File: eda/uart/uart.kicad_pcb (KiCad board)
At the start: 2 copper layers, 122.6 x 85.1 mm, 48 parts, among them J1 UART, J2 Bus expansion, U1 74HCT08, U10 74HCT574, U11 74HCT595, U12 74HCT595, U13 CD74HCT40105E, U14 CD74HCT40105E, U16 74HCT14, U17 74HCT193, U18 74HCT32, U2 74HCT14, U3 74HCT193, U4 74HCT193, U5 74HCT165, U6 74HCT165, U7 74HCT139, U8 CD74HCT40105E, U9 CD74HCT40105E, X1 1.8xx

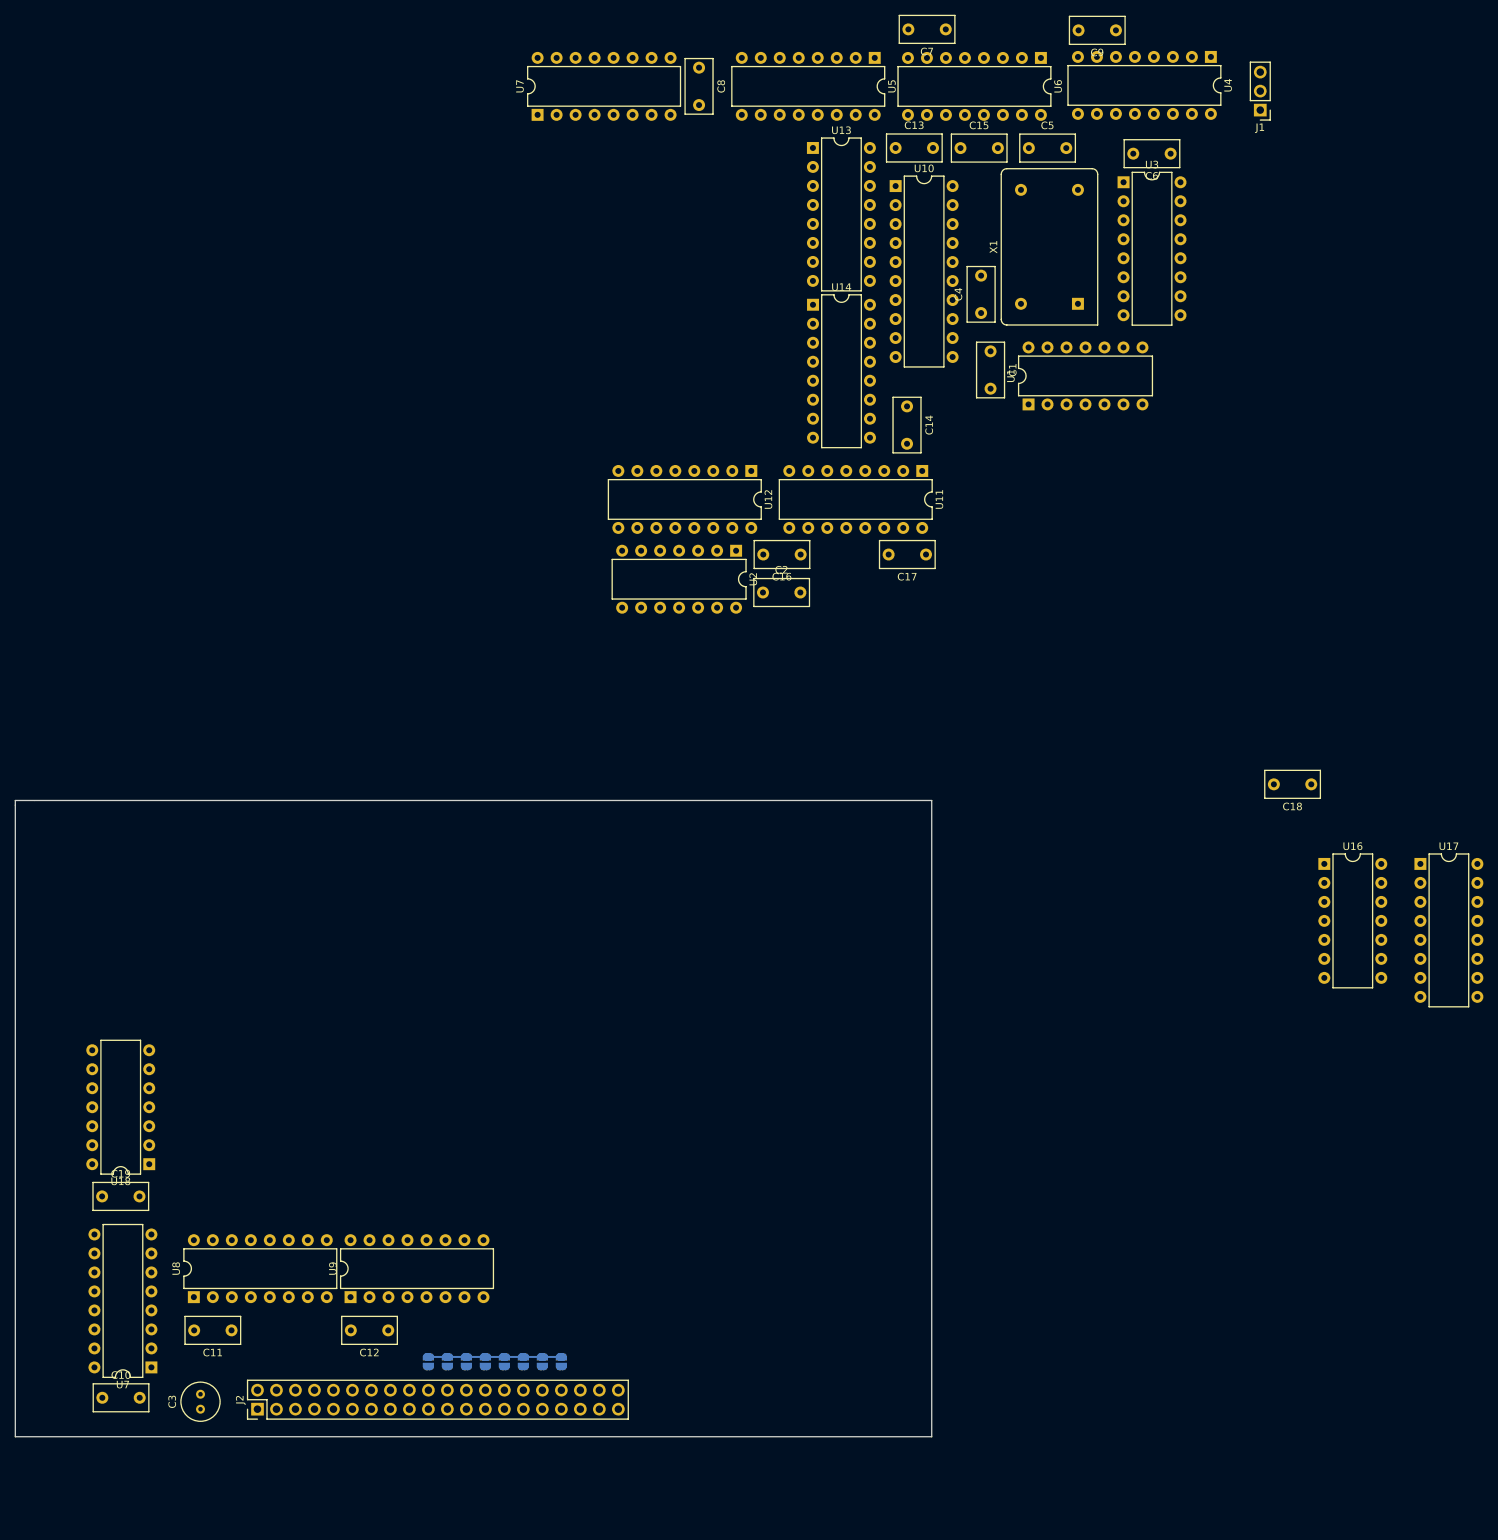
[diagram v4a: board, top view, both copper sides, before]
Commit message: Convert expansion breakout to kicad
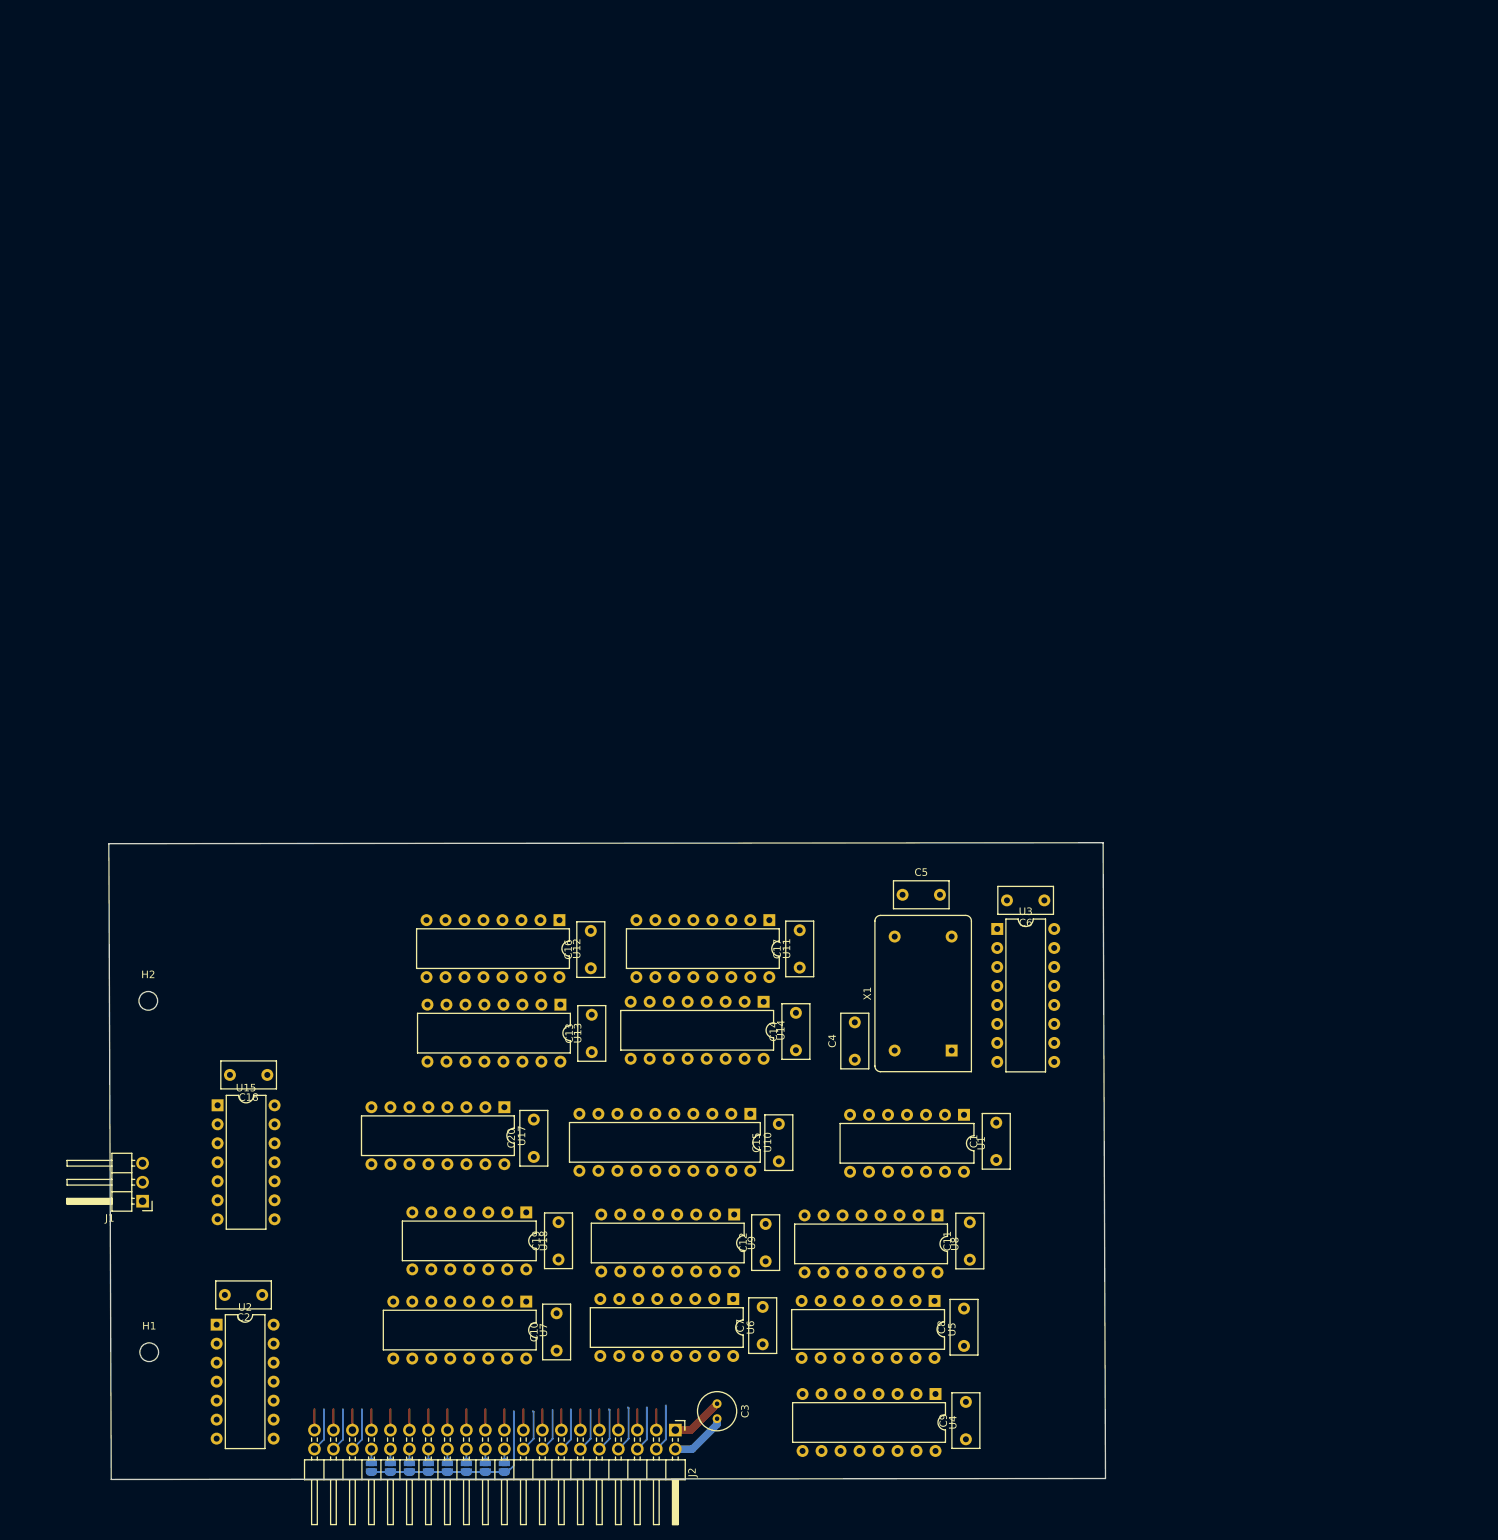
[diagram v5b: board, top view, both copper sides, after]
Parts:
- removed U16: 74HCT14, Package_DIP:DIP-14_W7.62mm
- removed the U7 at (95.9, -30.1)
- added C20: 0.1uf, Capacitor_THT:C_Rect_L7.2mm_W3.5mm_P5.00mm_FKS2_FKP2_MKS2_MKP2, F.Cu at (95.4, 109.3)
- added H1: Bracket mounting, MountingHole:MountingHole_2.5mm, F.Cu at (43.9, 135.4)
- added H2: Bracket mounting, MountingHole:MountingHole_2.5mm, F.Cu at (43.8, 88.4)
- added U15: 74HCT00, Package_DIP:DIP-14_W7.62mm, F.Cu at (53.1, 102.4)
- J1: footprint Connector_PinHeader_2.54mm:PinHeader_1x03_P2.54mm_Vertical -> Connector_PinHeader_2.54mm:PinHeader_1x03_P2.54mm_Horizontal
- J2: footprint Connector_PinHeader_2.54mm:PinHeader_2x20_P2.54mm_Vertical -> Connector_PinHeader_2.54mm:PinHeader_2x20_P2.54mm_Horizontal
- moved J1 208.9 mm to (43.1, 115.2)
- moved C9 189.5 mm to (153.2, 147.0), turned to 90 degrees
- moved U4 182.6 mm to (149.1, 141.0)
- moved C7 177.6 mm to (126.0, 134.3), turned to 90 degrees
- moved C8 174.6 mm to (152.9, 134.5), turned to 90 degrees
- moved U6 171.0 mm to (122.0, 128.3)
- moved U5 166.4 mm to (149.0, 128.5)
- moved C18 144.9 mm to (59.7, 98.3)
- moved C15 137.7 mm to (128.1, 109.9), turned to 90 degrees
- moved C13 127.6 mm to (103.1, 95.2), turned to 90 degrees
- moved U17 126.8 mm to (91.4, 102.6), turned to -90 degrees
- moved U10 125.6 mm to (124.3, 103.5), turned to -90 degrees
- moved U2 124.7 mm to (53.0, 131.7), turned to 0 degrees
- moved U13 119.4 mm to (98.9, 88.9), turned to -90 degrees
- moved C2 115.4 mm to (59.1, 127.7), turned to 180 degrees
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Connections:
- U13 pad 10: /Expansion header/D3 -> /recieve/FIFO Recieve/D3
- U13 pad 11: /Expansion header/D2 -> /recieve/FIFO Recieve/D2
- U13 pad 12: /Expansion header/D1 -> /recieve/FIFO Recieve/D1
- U13 pad 13: /Expansion header/D0 -> /recieve/FIFO Recieve/D0
- U14 pad 10: /Expansion header/D7 -> /recieve/FIFO Recieve/D7
- U14 pad 11: /Expansion header/D6 -> /recieve/FIFO Recieve/D6
- U14 pad 12: /Expansion header/D5 -> /recieve/FIFO Recieve/D5
- U14 pad 13: /Expansion header/D4 -> /recieve/FIFO Recieve/D4
- U2 pad 3: (no net) -> Net-(U4-QD)
- U2 pad 4: (no net) -> Net-(U7B-E)
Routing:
- net /Expansion header/~{CS}: track 18.9 -> 26.7 mm
- net GND: track 0.00 -> 7.72 mm
- net VCC: track 0.00 -> 7.05 mm
- net /Expansion header/D0: track 0.00 -> 6.37 mm
- net /Expansion header/D2: track 0.00 -> 6.19 mm
- net /Expansion header/D1: track 0.00 -> 6.11 mm
- net /Expansion header/D3: track 0.00 -> 5.94 mm
- net /Expansion header/~{RST}: track 0.00 -> 5.86 mm
- net /Expansion header/~{NMI}: track 0.00 -> 5.86 mm
- net /Expansion header/~{IRQ}: track 0.00 -> 5.86 mm
- net /Expansion header/D5: track 0.00 -> 5.86 mm
- net /Expansion header/D6: track 0.00 -> 5.80 mm
- net /Expansion header/D4: track 0.00 -> 5.80 mm
- net /Expansion header/D7: track 0.00 -> 5.68 mm
- net /Expansion header/~{DMA}: track 0.00 -> 2.79 mm
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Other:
- board size 122.6 x 85.1 mm -> 133.3 x 85.2 mm
- board text added: "0"
- board text added: "1"
- board text added: "2"
- board text added: "3"
- board text added: "4"
- board text added: "5"
- board text added: "6"
- board text added: "7"

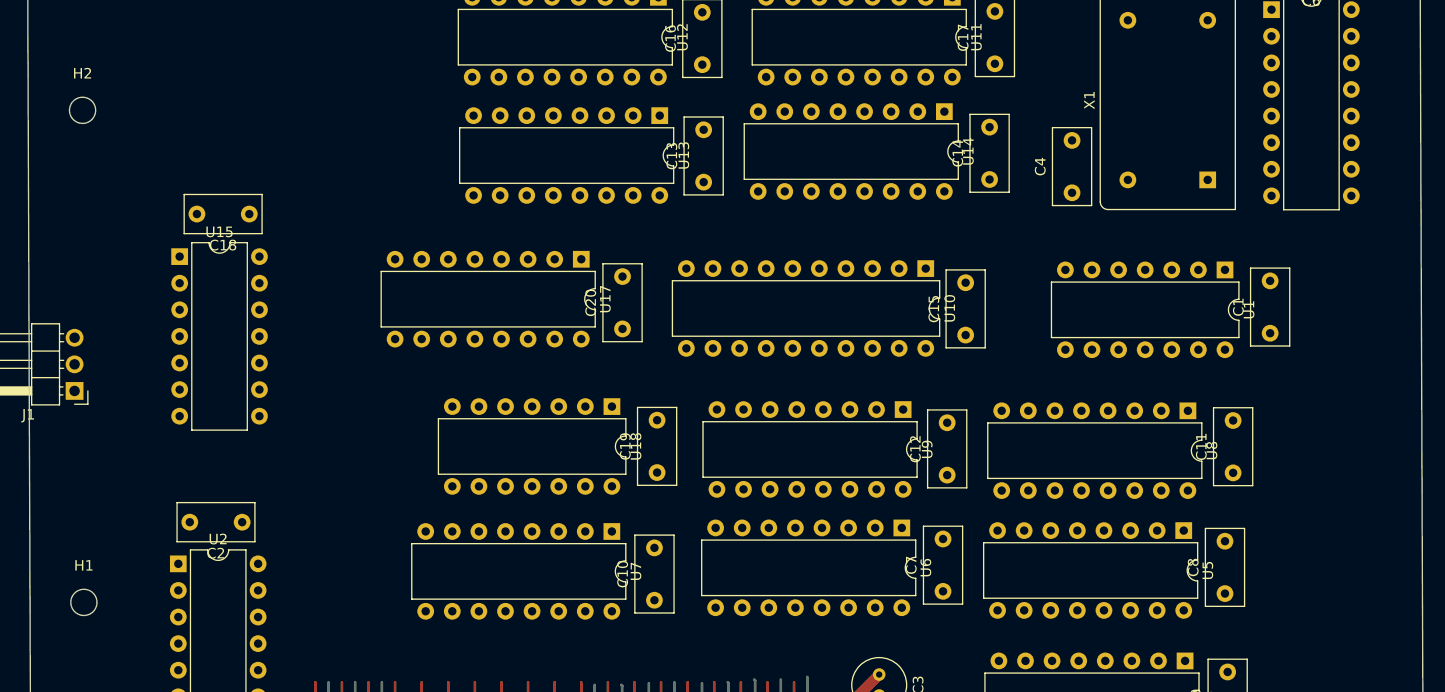
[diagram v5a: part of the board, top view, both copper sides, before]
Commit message: Update UART transmit logic
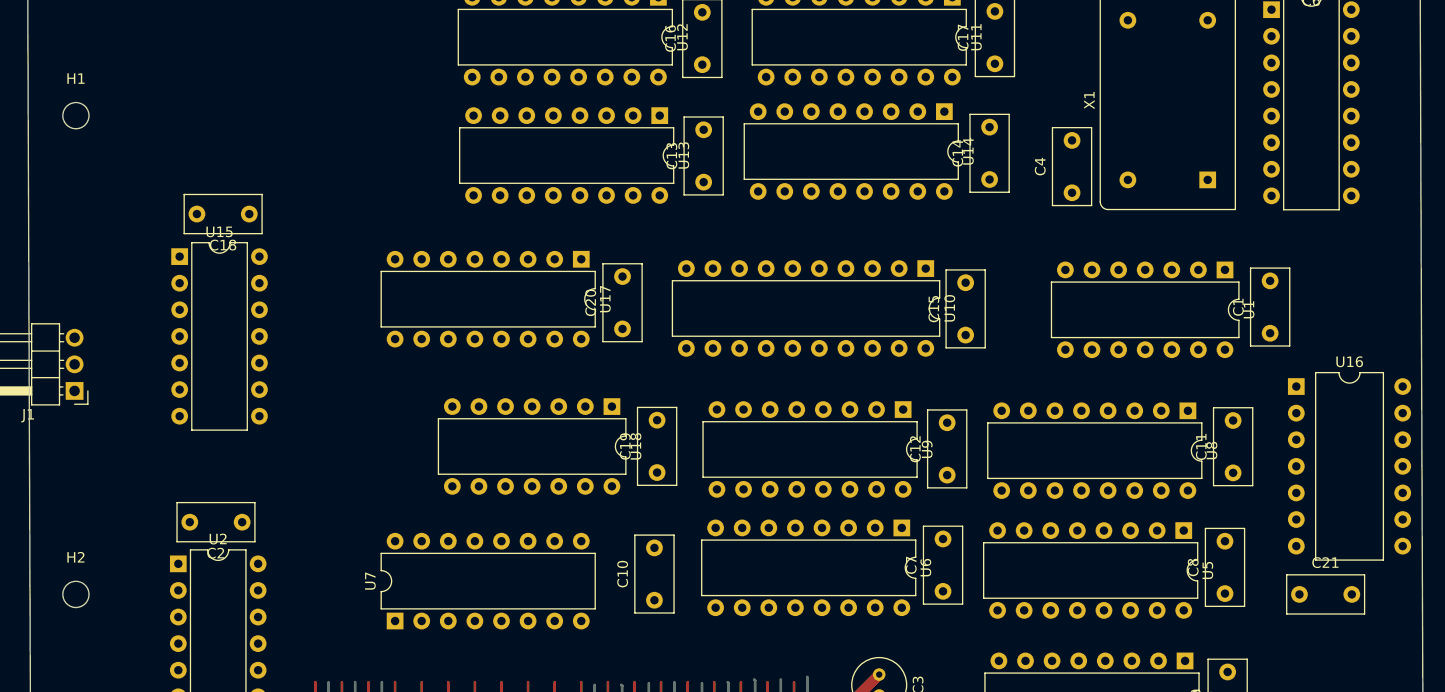
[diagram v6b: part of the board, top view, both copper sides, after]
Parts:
- added C21: 0.1uf, Capacitor_THT:C_Rect_L7.2mm_W3.5mm_P5.00mm_FKS2_FKP2_MKS2_MKP2, F.Cu at (160.0, 134.6)
- added U16: 74HCT74, Package_DIP:DIP-14_W10.16mm, F.Cu at (159.7, 114.8)
- H1, H2: value Bracket mounting -> MountingHole
- moved H1 46.5 mm to (43.2, 88.9)
- moved H2 46.2 mm to (43.2, 134.6)
- moved U7 22.4 mm to (73.7, 137.2), turned to 90 degrees
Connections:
- C4 pad 2: Net-(U3-UP) -> Net-(U3-DOWN)
- C5 pad 1: Net-(U3-UP) -> Net-(U3-DOWN)
- U2 pad 3: Net-(U4-QD) -> (no net)
- U2 pad 4: Net-(U7B-E) -> (no net)
- U3 pad 11: VCC -> Net-(U16A-C)
- U3 pad 13: /clock/UartClock -> Net-(U16A-C)
- U3 pad 4: unconnected-(U3-DOWN-Pad4) -> Net-(U3-DOWN)
- U3 pad 5: Net-(U3-UP) -> unconnected-(U3-UP-Pad5)
- U3 pad 9: GND -> VCC
- U4 pad 11: /transmit/FIFO Transmit/DOR -> /transmit/~{LatchShiftRegisters}
- U4 pad 13: /transmit/FIFO Transmit/SO -> Net-(U16B-~{R})
- U4 pad 2: Net-(U4-QB) -> unconnected-(U4-QB-Pad2)
- U4 pad 3: Net-(U4-QA) -> unconnected-(U4-QA-Pad3)
- U4 pad 7: Net-(U4-QD) -> unconnected-(U4-QD-Pad7)
- U5 pad 15: GND -> /transmit/~{ClockEnable}
- U6 pad 15: GND -> /transmit/~{ClockEnable}
- U7 pad 13: Net-(U4-QA) -> unconnected-(U7B-A1-Pad13)
- U7 pad 14: Net-(U4-QB) -> unconnected-(U7B-A0-Pad14)
- U7 pad 15: Net-(U7B-E) -> unconnected-(U7B-E-Pad15)
- U7 pad 9: /transmit/~{LatchShiftRegisters} -> unconnected-(U7B-O3-Pad9)
- U8 pad 15: /transmit/FIFO Transmit/SO -> /transmit/~{ClockEnable}
- U9 pad 15: /transmit/FIFO Transmit/SO -> /transmit/~{ClockEnable}
- X1 pad 8: Net-(U3-UP) -> Net-(U3-DOWN)
